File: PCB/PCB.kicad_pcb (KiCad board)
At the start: 4 copper layers, 104.1 x 104.1 mm, 113 parts, among them J1 Conn_01x06_Female, J3 DB25_Receptacle_MountingHoles, U1 Hx711, U10 Hx711, U11 Hx711, U12 Hx711, U13 74HC165, U15 LT3042xMSE, U16 74HC165, U2 Hx711, U3 Hx711, U4 Hx711, U5 Hx711, U6 Hx711, U7 Hx711, U8 Hx711, U9 Hx711

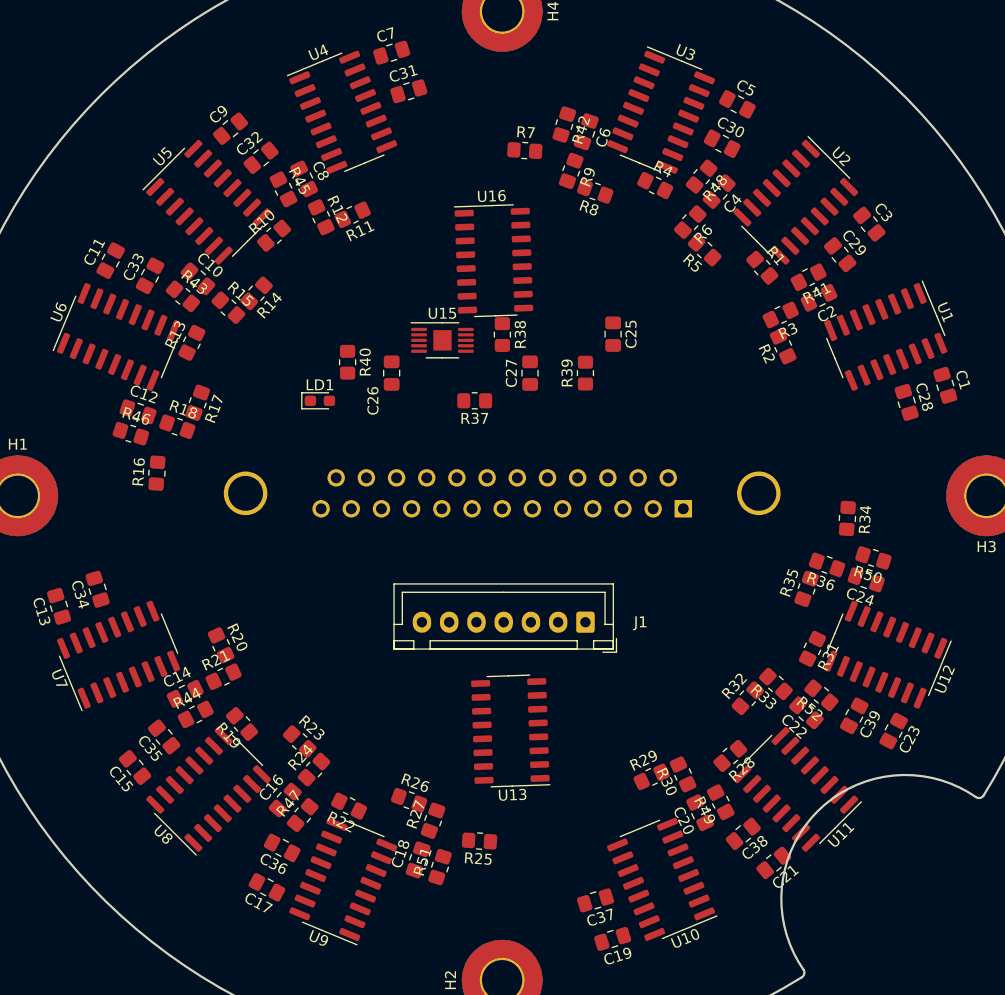
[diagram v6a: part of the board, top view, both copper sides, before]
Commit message: PCB routing
Started work on two ground planes and wiring each section to each other.
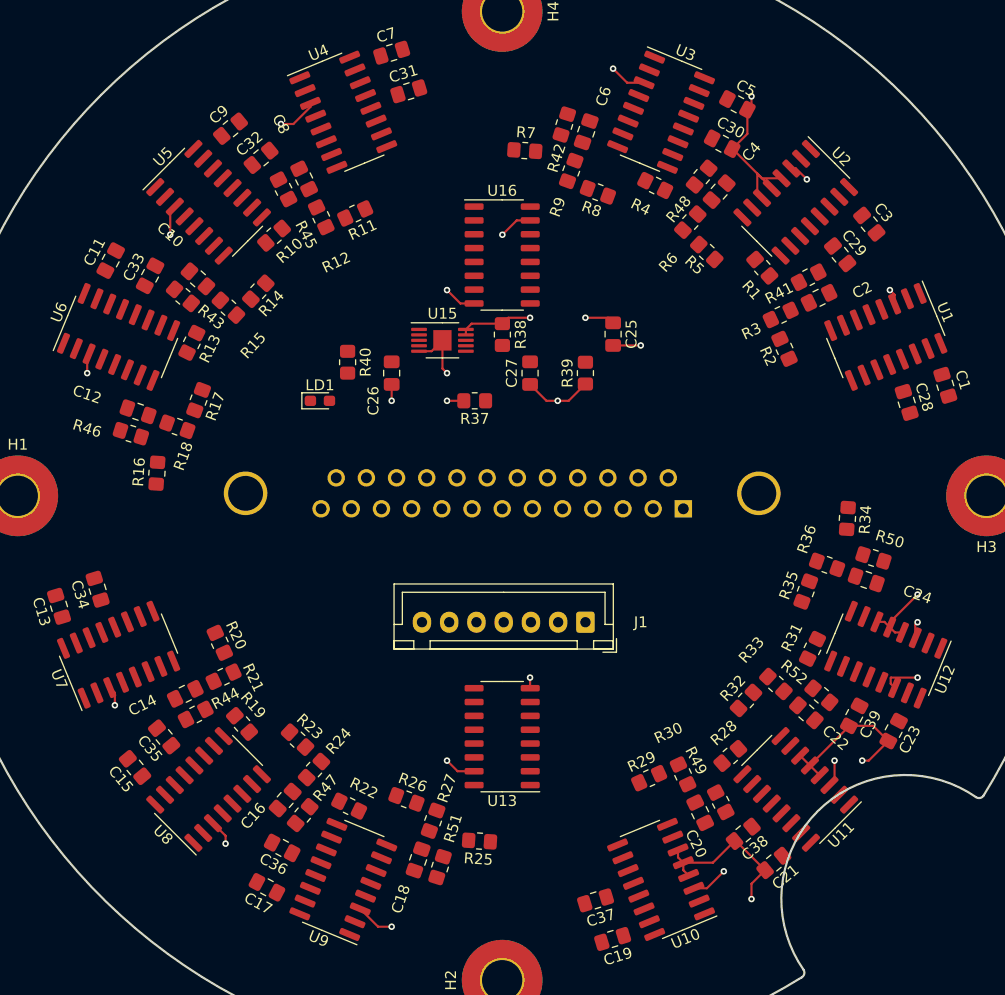
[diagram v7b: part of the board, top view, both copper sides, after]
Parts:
- moved U16 0.92 mm to (160.0, 67.9), turned to 0 degrees
- moved U13 0.92 mm to (160.0, 112.1), turned to 180 degrees
- moved R14 0.25 mm to (137.6, 71.2), turned to -133 degrees
- moved R32 0.25 mm to (182.4, 108.8), turned to 47 degrees
- moved R23 0.25 mm to (141.2, 112.4), turned to -43 degrees
- moved R5 0.25 mm to (178.8, 67.6), turned to 137 degrees
- moved R11 0.25 mm to (146.5, 64.1), turned to -155.5 degrees
- moved R29 0.25 mm to (173.5, 115.9), turned to 24.5 degrees
- moved R2 0.25 mm to (185.9, 76.5), turned to 114.5 degrees
- moved R20 0.25 mm to (134.1, 103.5), turned to -65.5 degrees
- moved R17 0.25 mm to (132.1, 81.2), turned to -110.5 degrees
- moved R35 0.25 mm to (187.9, 98.8), turned to 69.5 degrees
- moved R8 0.25 mm to (168.8, 62.1), turned to 159.5 degrees
- moved R26 0.25 mm to (151.2, 117.9), turned to -20.5 degrees
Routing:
- net GND: track 0.00 -> 83.8 mm, vias 0 -> 14
- net 4.5V: track 0.00 -> 39.6 mm, vias 0 -> 14
- added copper zone on In1.Cu, net 4.5V
- added copper zone on In2.Cu, net GND

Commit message: updated PCB
Current version with errors
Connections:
- J3 pad 10: /H14P -> /H11N
- J3 pad 11: /H13P -> /H3P
- J3 pad 12: /H11P -> /H3N
- J3 pad 14: /HP -> /H14P
- J3 pad 15: /H1P -> /HN
- J3 pad 16: /H2P -> /HP
- J3 pad 17: /H3P -> /H12N
- J3 pad 18: /H4P -> /H12P
- J3 pad 19: /H5P -> /H1N
- J3 pad 2: /HN -> /H14N
- J3 pad 20: /H12P -> /H1P
- J3 pad 21: /H9P -> /H9N
- J3 pad 22: /H14N -> /H9P
- J3 pad 23: /H13N -> /H2N
- J3 pad 24: /H11N -> /H2P
- J3 pad 3: /H1N -> /H5P
- J3 pad 4: /H2N -> /H5N
- J3 pad 5: /H3N -> /H13P
- J3 pad 6: /H4N -> /H13N
- J3 pad 7: /H5N -> /H4P
- J3 pad 8: /H12N -> /H4N
- J3 pad 9: /H9N -> /H11P
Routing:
- net GND: track 83.8 -> 155.7 mm, vias 14 -> 27
- net +5V: track 0.00 -> 21.7 mm, vias 0 -> 2
- net Net-(U9-INA-): track 0.00 -> 5.83 mm
- net Net-(U9-INA+): track 0.00 -> 5.34 mm
- net /H4N: track 0.00 -> 2.13 mm
- added copper zone on B.Cu, net +5V
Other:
- board size 104.1 x 104.1 mm -> 2768.4 x 3037 mm
